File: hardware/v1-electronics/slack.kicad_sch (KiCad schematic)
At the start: 143 parts, among them SW1 SW_Push_45deg, SW10 SW_Push_45deg, SW11 SW_Push_45deg, SW12 SW_Push_45deg, SW13 SW_Push_45deg, SW14 SW_Push_45deg, SW15 SW_Push_45deg, SW16 SW_Push_45deg, SW17 SW_Push_45deg, SW18 SW_Push_45deg, SW19 SW_Push_45deg, SW2 SW_Push_45deg, SW20 SW_Push_45deg, SW23 SW_Push_45deg, SW24 SW_Push_45deg, SW25 SW_Push_45deg, SW26 SW_Push_45deg, SW27 SW_Push_45deg, SW28 SW_Push_45deg, SW29 SW_Push_45deg, SW3 SW_Push_45deg, SW30 SW_Push_45deg, SW31 SW_Push_45deg, SW32 SW_Push_45deg, SW33 SW_Push_45deg, SW34 SW_Push_45deg, SW37 SW_Push_45deg, SW38 SW_Push_45deg, SW39 SW_Push_45deg, SW4 SW_Push_45deg, SW40 SW_Push_45deg, SW41 SW_Push_45deg, SW42 SW_Push_45deg, SW43 SW_Push_45deg, SW44 SW_Push_45deg, SW45 SW_Push_45deg, SW46 SW_Push_45deg, SW47 SW_Push_45deg, SW48 SW_Push_45deg, SW5 SW_Push_45deg, SW51 SW_Push_45deg, SW52 SW_Push_45deg, SW53 SW_Push_45deg, SW54 SW_Push_45deg, SW55 SW_Push_45deg, SW56 SW_Push_45deg, SW57 SW_Push_45deg, SW58 SW_Push_45deg, SW59 SW_Push_45deg, SW6 SW_Push_45deg, SW60 SW_Push_45deg, SW61 SW_Push_45deg, SW62 SW_Push_45deg, SW63 SW_Push, SW66 SW_Push, SW67 SW_Push_45deg, SW68 SW_Push_45deg, SW69 SW_Push_45deg, SW70 SW_Push_45deg, SW71 SW_Push_45deg, SW72 SW_Push_45deg, SW9 SW_Push_45deg, U1 MDBT50Q-U1MV2

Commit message: feat(v1 hardware): complete matrix schematic
I added the filters for the all the encoders

I will need to add the latching buttons in the future. For now the
latches have been excluding from the schematic all together. I think the
best way to add them would be to add another row to the matrix, that is
only latches.
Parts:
- added C1, C10, C11, C12, C13, C14, C15, C16, C17, C18, C19, C2, C20, C3, C4, C5, C6, C7, C8, C9: C_Small, symbol Device:C_Small
- added R1, R10, R11, R12, R13, R14, R15, R16, R17, R18, R19, R2, R20, R21, R22, R23, R24, R25, R26, R27, R28, R29, R3, R30, R31, R32, R33, R34, R35, R36, R37, R38, R39, R4, R40, R5, R6, R7, R8, R9: R_Small, symbol Device:R_Small
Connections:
- net at RE6/SW36.A: now also R21.1, R22.2
- net at RE6/SW36.B: now also R23.2, R24.1
- net GND: now reaches RE6/SW36.C
- net GND: now also RE1/SW7.C, RE10.C, RE2/SW8.C, RE3/SW21.C, RE4/SW22.C, RE5/SW35.C, RE7/SW49.C, RE8/SW50.C, RE9.C, C1.1, C10.2, C11.1, C12.2, C13.1, C14.2, C15.1, C16.2, C17.1, C18.2, C19.1, C2.2, C20.2, C3.1, C4.2, C5.1, C6.2, C7.1, C8.2, C9.1
- net at RE1/SW7.A: now also R3.1, R4.2
- net at RE1/SW7.B: now also R1.2, R2.2
- net at RE3/SW21.A: now also R11.1, R12.2
- net at RE3/SW21.B: now also R10.1, R9.2
- net at RE7/SW49.A: now also R26.2, R28.2
- net at RE7/SW49.B: now also R25.2, R27.2
- net at RE5/SW35.A: now also R19.2, R20.2
- net at RE5/SW35.B: now also R17.2, R18.2
- net at RE2/SW8.A: now also R5.2, R6.2
- net at RE2/SW8.B: now also R7.1, R8.2
- net at RE10.A: now also R37.2, R38.2
- net at RE10.B: now also R39.1, R40.1
- net at RE4/SW22.A: now also R13.2, R14.1
- net at RE4/SW22.B: now also R15.2, R16.2
- net at RE8/SW50.A: now also R29.2, R30.2
- net at RE8/SW50.B: now also R31.1, R32.2
- net at RE9.A: now also R35.1, R36.2
- net at RE9.B: now also R33.2, R34.2
- new net RE10_A-Channel: C19.2, C20.1, R38.1, R40.2
- new net RE1_A-Channel: C2.1, R4.1
- new net RE1_B-Channel: C1.2, R2.1
- new net RE2_A-Channel: C3.2, R6.1
- new net RE2_B-Channel: C4.1, R8.1
- new net RE3_A-Channel: C6.1, R12.1
- new net RE3_B-Channel: C5.2, R10.2
- new net RE4_A-Channel: C7.2, R14.2
- new net RE4_B-Channel: C8.1, R16.1
- new net RE5_A-Channel: C10.1, R20.1
- new net RE5_B-Channel: C9.2, R18.1
- new net RE6_A-Channel: C11.2, R22.1
- new net RE6_B-Channel: C12.1, R24.2
- new net RE7_A-Channel: C14.1, R28.1
- new net RE7_B-Channel: C13.2, R27.1
- new net RE8_A-Channel: C15.2, R30.1
- new net RE8_B-Channel: C16.1, R32.1
- new net RE9_A-Channel: C18.1, R36.1
- new net RE9_B-Channel: C17.2, R34.1
- new net VDD: R1.1, R11.2, R13.1, R15.1, R17.1, R19.1, R21.2, R23.1, R25.1, R26.1, R29.1, R3.2, R31.2, R33.1, R35.2, R37.1, R39.2, R5.1, R7.2, R9.1
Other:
- moved on the sheet: D1, D10, D11, D12, D13, D14, D15, D16, D17, D18, D19, D2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

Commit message: feat(v1 hardware): added usb-c and select mcu power mode
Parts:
- removed C1, C10, C11, C12, C13, C14, C15, C16, C17, C18, C19, C2, C20, C3, C4, C5, C6, C7, C8, C9: C_Small, symbol Device:C_Small
- removed D1, D10, D11, D12, D13, D14, D15, D16, D17, D18, D19, D2, D20, D21, D22, D23, D24, D25, D26, D27, D28, D29, D3, D30, D31, D32, D33, D34, D35, D36, D37, D38, D39, D4, D40, D41, D42, D43, D44, D45, D46, D47, D48, D49, D5, D50, D51, D52, D53, D54, D55, D56, D57, D58, D59, D6, D60, D61, D62, D63, D64, D65, D66, D67, D68, D69, D7, D70, D8, D9: D, symbol Device:D
- removed R1, R10, R11, R12, R13, R14, R15, R16, R17, R18, R19, R2, R20, R21, R22, R23, R24, R25, R26, R27, R28, R29, R3, R30, R31, R32, R33, R34, R35, R36, R37, R38, R39, R4, R40, R5, R6, R7, R8, R9: R_Small, symbol Device:R_Small
- removed RE1/SW7, RE2/SW8, RE3/SW21, RE4/SW22, RE5/SW35, RE6/SW36, RE7/SW49, RE8/SW50: RotaryEncoder_Switch, symbol Device:RotaryEncoder_Switch
- removed RE10, RE9: RotaryEncoder, symbol Device:RotaryEncoder
- removed SW1, SW10, SW11, SW12, SW13, SW14, SW15, SW16, SW17, SW18, SW19, SW2, SW20, SW23, SW24, SW25, SW26, SW27, SW28, SW29, SW3, SW30, SW31, SW32, SW33, SW34, SW37, SW38, SW39, SW4, SW40, SW41, SW42, SW43, SW44, SW45, SW46, SW47, SW48, SW5, SW51, SW52, SW53, SW54, SW55, SW56, SW57, SW58, SW59, SW6, SW60, SW61, SW62, SW67, SW68, SW69, SW70, SW71, SW72, SW9: SW_Push_45deg, symbol Switch:SW_Push_45deg
- removed SW63, SW66: SW_Push, symbol Switch:SW_Push
- removed U1: MDBT50Q-U1MV2, RF_Module:Raytac_MDBT50Q, symbol RF_Module:MDBT50Q-U1MV2
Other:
- added sheet Switch Matrix (switch_matrix.kicad_sch)
- added sheet microcontroller (microcontroller.kicad_sch)

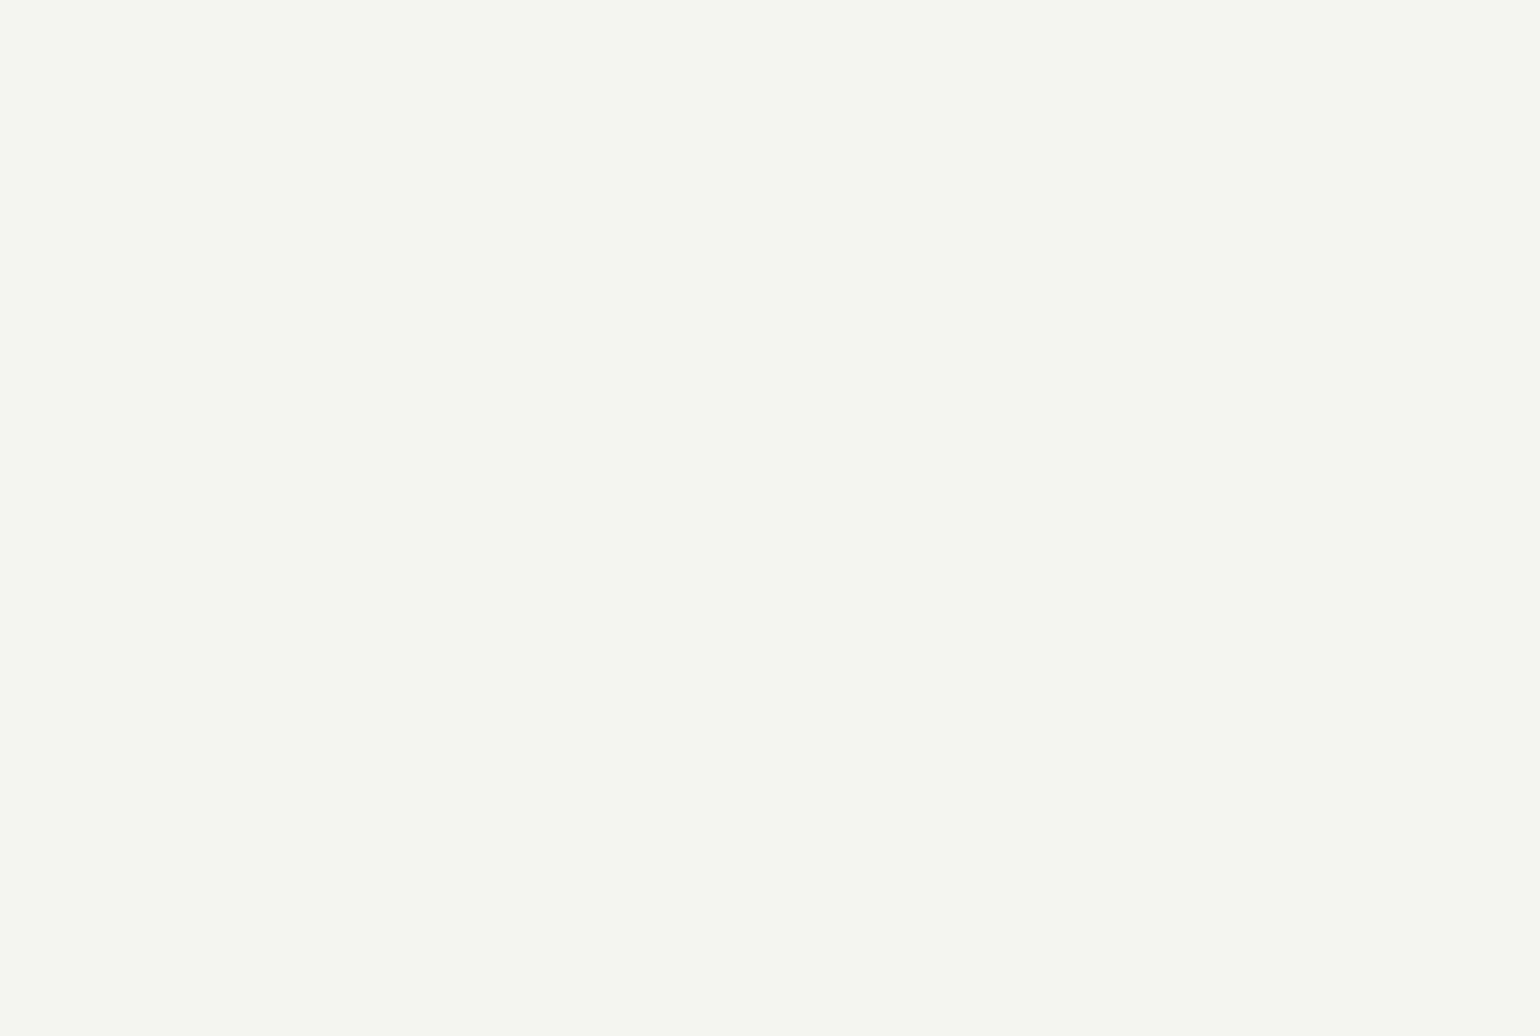
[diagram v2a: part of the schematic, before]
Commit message: feat(v1 hardware): LED Matrix
- added symbols and footprints for leds and their matrix ic.
- modified symbols for leds.
- started schematic for matrix ic and led matrix
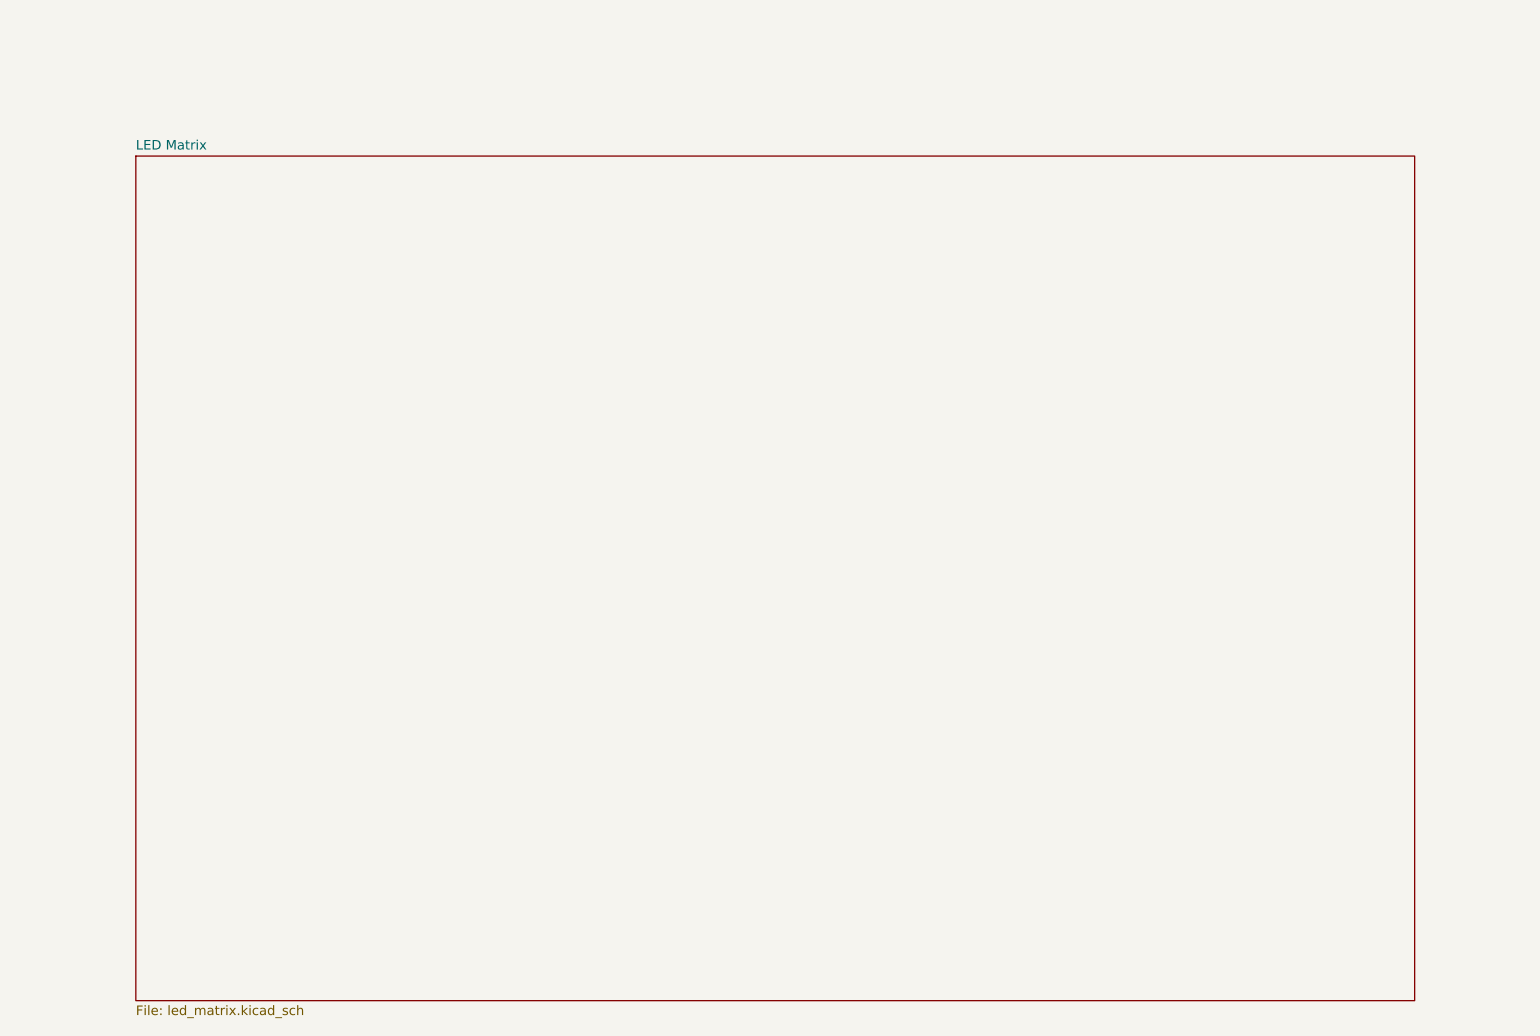
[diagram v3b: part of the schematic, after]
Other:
- added sheet LED Matrix (led_matrix.kicad_sch)
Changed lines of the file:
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@@
+		)
+	)
+	(sheet
+		(at 274.955 207.01)
+		(size 170.18 112.395)
+		(exclude_from_sim no)
+		(in_bom yes)
+		(on_board yes)
+		(dnp no)
+		(fields_autoplaced yes)
+		(stroke
+			(width 0.1524)
+			(type solid)
+		)
+		(fill
+			(color 0 0 0 0)
+		)
+		(property "Sheetname" "LED Matrix"
+			(at 274.955 206.2984 0)
+			(show_name no)
+			(do_not_autoplace no)
+			(effects
+				(font
+					(size 1.27 1.27)
+				)
+				(justify left bottom)
+			)
+		)
+		(property "Sheetfile" "led_matrix.kicad_sch"
+			(at 274.955 319.9896 0)
+			(show_name no)
+			(do_not_autoplace no)
+			(effects
+				(font
+					(size 1.27 1.27)
+				)
+				(justify left top)
+			)
+		)
+		(instances
+			(project "slack"
+				(path "/504df67f-9f45-483f-90c8-f14c049b6b02"
+					(page "4")
+				)
+			)
 		)
 	)

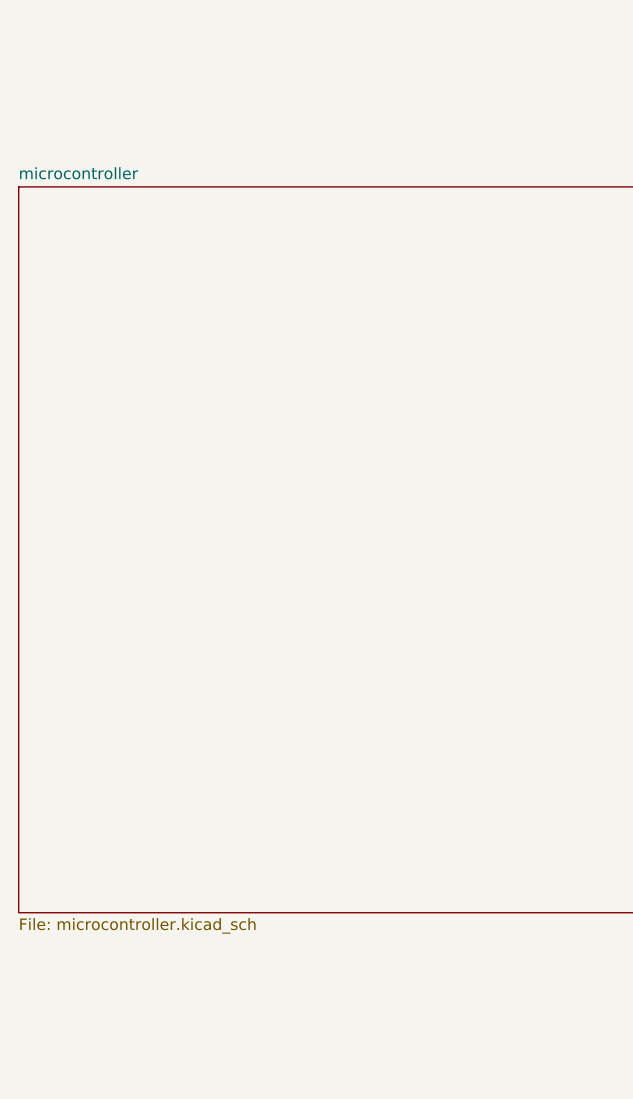
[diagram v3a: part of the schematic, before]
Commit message: feat(v1 hardware): LED Matrix refactor start
- refactored RGBW LED schematic symbol.
- realize that IS31FL3741A will need to be replaced.
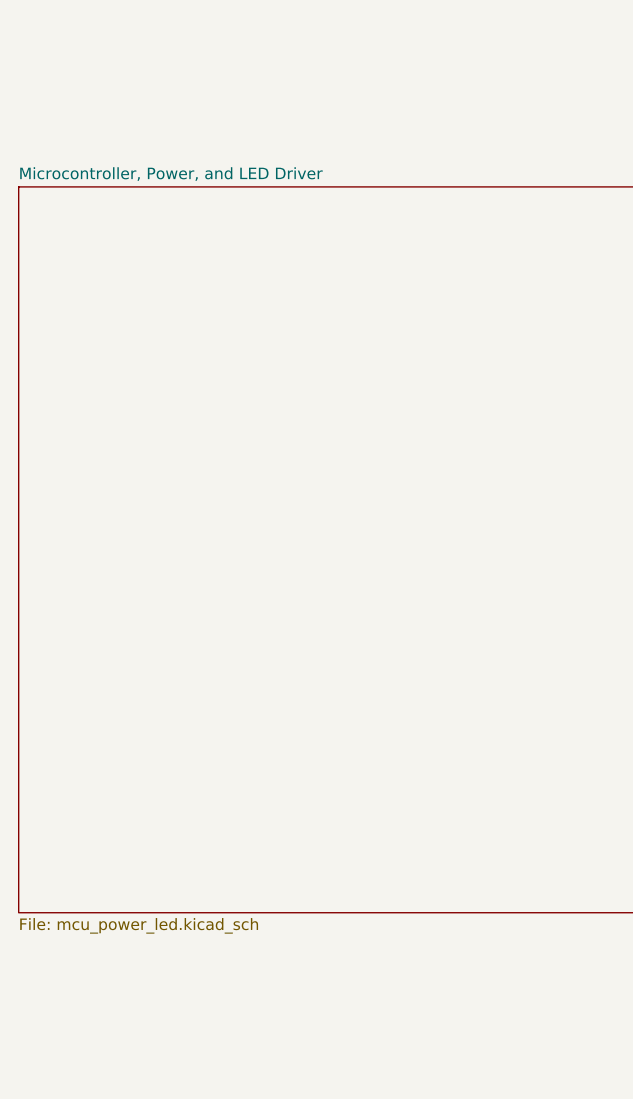
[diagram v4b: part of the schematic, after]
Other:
- sheet microcontroller renamed Microcontroller, Power, and LED Driver
- sheet Microcontroller, Power, and LED Driver: file microcontroller.kicad_sch -> mcu_power_led.kicad_sch
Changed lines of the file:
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@@
 			(color 0 0 0 0)
 		)
-		(property "Sheetname" "microcontroller"
+		(property "Sheetname" "Microcontroller, Power, and LED Driver"
 			(at 59.055 154.2284 0)
 			(show_name no)
@@
 			)
 		)
-		(property "Sheetfile" "microcontroller.kicad_sch"
+		(property "Sheetfile" "mcu_power_led.kicad_sch"
 			(at 59.055 236.1696 0)
 			(show_name no)

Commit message: feat(v1 hardware): Add new LED Matrix driver
- added the symbol for 3733
- added circuit for 3733
- have not removed: old matrix and 3741A symbol & circuits
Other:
- sheet Microcontroller, Power, and LED Driver renamed Power Train
- added sheet Controller ICs (controller.kicad_sch)
- sheet Power Train: file mcu_power_led.kicad_sch -> power.kicad_sch
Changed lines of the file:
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@@
 	(paper "A2")
 	(sheet
-		(at 314.325 46.355)
-		(size 145.415 97.155)
+		(at 159.385 15.875)
+		(size 145.415 80.645)
 		(exclude_from_sim no)
 		(in_bom yes)
 		(on_board yes)
 		(dnp no)
-		(fields_autoplaced yes)
 		(stroke
-			(width 0.1524)
+			(width 0.5)
 			(type solid)
 		)
@@
 		)
 		(property "Sheetname" "Switch Matrix"
-			(at 314.325 45.6434 0)
+			(at 160.02 22.86 0)
 			(show_name no)
 			(do_not_autoplace no)
 			(effects
 				(font
-					(size 1.27 1.27)
+					(size 5 5)
+					(thickness 1)
+					(bold yes)
 				)
 				(justify left bottom)
@@
 		)
 		(property "Sheetfile" "switch_matrix.kicad_sch"
-			(at 314.325 144.0946 0)
+			(at 162.56 91.44 0)
 			(show_name no)
 			(do_not_autoplace no)
 			(effects
 				(font
-					(size 1.27 1.27)
+					(size 2 2)
 				)
 				(justify left top)
@@
 	)
 	(sheet
-		(at 59.055 154.94)
-		(size 149.225 80.645)
+		(at 13.335 15.24)
+		(size 144.145 80.645)
 		(exclude_from_sim no)
 		(in_bom yes)
 		(on_board yes)
 		(dnp no)
-		(fields_autoplaced yes)
 		(stroke
-			(width 0.1524)
+			(width 0.5)
 			(type solid)
 		)
@@
 			(color 0 0 0 0)
 		)
-		(property "Sheetname" "Microcontroller, Power, and LED Driver"
-			(at 59.055 154.2284 0)
+		(property "Sheetname" "Power Train"
+			(at 35.56 20.32 0)
 			(show_name no)
 			(do_not_autoplace no)
 			(effects
 				(font
-					(size 1.27 1.27)
+					(size 5 5)
+					(thickness 0.254)
+					(bold yes)
 				)
-				(justify left bottom)
 			)
 		)
-		(property "Sheetfile" "mcu_power_led.kicad_sch"
-			(at 59.055 236.1696 0)
+		(property "Sheetfile" "power.kicad_sch"
+			(at 30.48 91.44 0)
 			(show_name no)
 			(do_not_autoplace no)
 			(effects
 				(font
-					(size 1.27 1.27)
+					(size 2 2)
+					(italic yes)
 				)
-				(justify left top)
 			)
 		)
@@
 	)
 	(sheet
-		(at 274.955 207.01)
-		(size 170.18 112.395)
+		(at 160.02 99.06)
+		(size 144.78 73.66)
 		(exclude_from_sim no)
 		(in_bom yes)
 		(on_board yes)
 		(dnp no)
-		(fields_autoplaced yes)
 		(stroke
-			(width 0.1524)
+			(width 0.5)
+			(type solid)
+		)
+		(fill
+			(color 0 0 0 0)
+		)
+		(property "Sheetname" "Controller ICs"
+			(at 160.02 106.68 0)
+			(show_name no)
+			(do_not_autoplace no)
+			(effects
+				(font
+					(size 5 5)
+					(thickness 0.254)
+					(bold yes)
+				)
+				(justify left bottom)
+			)
+		)
+		(property "Sheetfile" "controller.kicad_sch"
+			(at 162.56 167.64 0)
+			(show_name no)
+			(do_not_autoplace no)
+			(effects
+				(font
+					(size 2 2)
+					(italic yes)
+				)
+				(justify left top)
+			)
+		)
+		(instances
+			(project "slack"
+				(path "/504df67f-9f45-483f-90c8-f14c049b6b02"
+					(page "5")
+				)
+			)
+		)
+	)
+	(sheet
+		(at 13.335 97.79)
+		(size 144.145 74.93)
+		(exclude_from_sim no)
+		(in_bom yes)
+		(on_board yes)
+		(dnp no)
+		(stroke
+			(width 0.5)
 			(type solid)
 		)
@@
 		)
 		(property "Sheetname" "LED Matrix"
-			(at 274.955 206.2984 0)
+			(at 12.7 106.68 0)
 			(show_name no)
 			(do_not_autoplace no)
 			(effects
 				(font
-					(size 1.27 1.27)
+					(size 5 5)
+					(thickness 1)
+					(bold yes)
 				)
 				(justify left bottom)
@@
 		)
 		(property "Sheetfile" "led_matrix.kicad_sch"
-			(at 274.955 319.9896 0)
+			(at 15.24 167.64 0)
 			(show_name no)
 			(do_not_autoplace no)
 			(effects
 				(font
-					(size 1.27 1.27)
+					(size 2 2)
 				)
 				(justify left top)
